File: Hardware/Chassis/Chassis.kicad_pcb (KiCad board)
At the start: 2 copper layers, 335.9 x 459.3 mm, 41 parts, among them J1 AC in, J11 Conn_01x04, J12 Conn_01x03, J13 Conn_01x04, J14 Conn_01x03, J2 Power relay trigger, J2 Relay power, J3 Digital In, J4 15V AC, J5 230V AC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

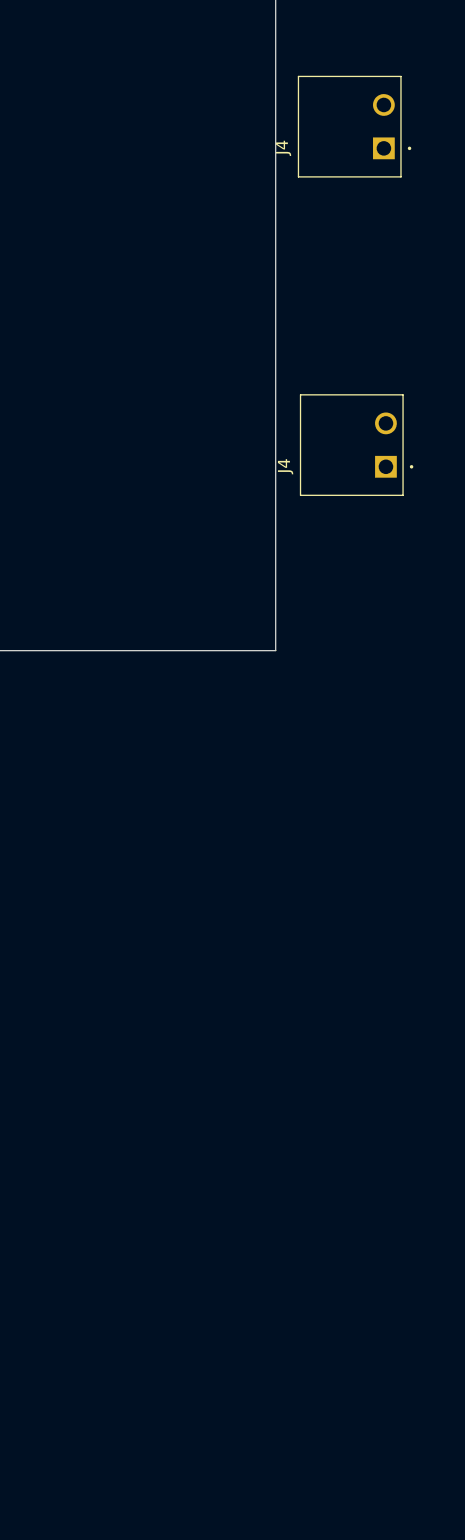
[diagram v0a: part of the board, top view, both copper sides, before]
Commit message: pcb splitout
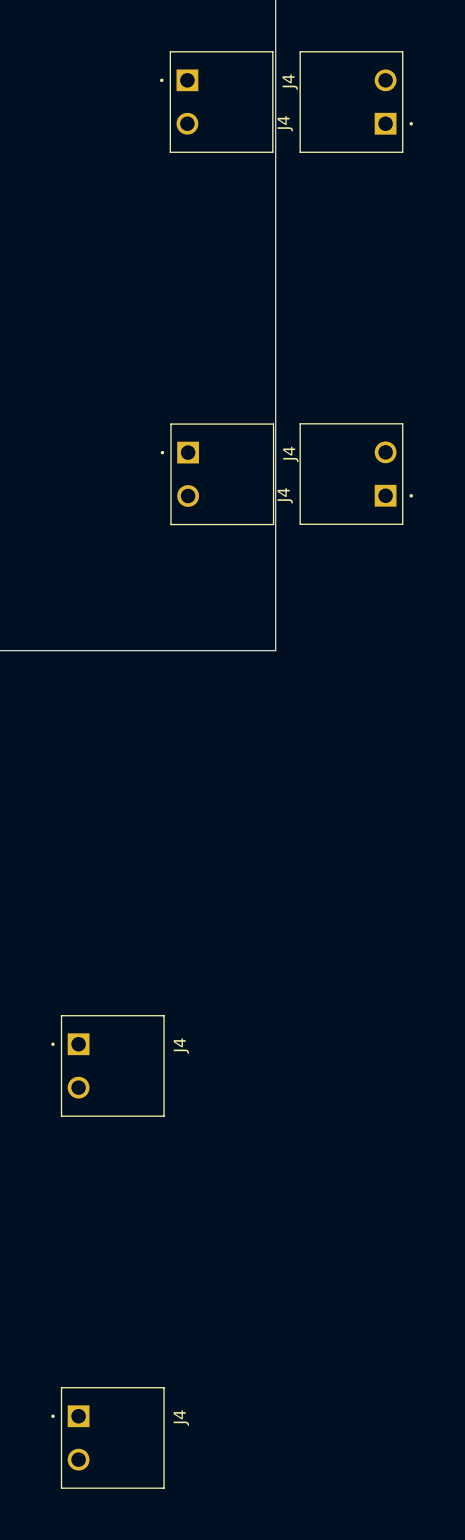
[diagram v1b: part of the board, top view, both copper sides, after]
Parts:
- added J4: 15V AC, THE_PREAMP_CONN_POWER_5_08:TBP01R1-508-02BK, F.Cu at (373.8, 253.7)
- added J4: 15V AC, THE_PREAMP_CONN_POWER_5_08:TBP01R1-508-02BK, F.Cu at (361.1, 366.6)
- added J4: 15V AC, THE_PREAMP_CONN_POWER_5_08:TBP01R1-508-02BK, F.Cu at (373.9, 297.3)
- added J4: 15V AC, THE_PREAMP_CONN_POWER_5_08:TBP01R1-508-02BK, F.Cu at (361.1, 410.1)
- moved J4 3.39 mm to (397.0, 302.4)
- moved J4 2.89 mm to (397.0, 258.8)

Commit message: gitignore test
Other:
- board text added: "backup test - delete later"
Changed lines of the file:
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@@
+		)
+	)
+	(gr_text "backup test - delete later"
+		(at 423.07 351.51 0)
+		(layer "F.Fab")
+		(effects
+			(font
+				(size 1 1)
+				(thickness 0.15)
+			)
+			(justify left bottom)
 		)
 	)
